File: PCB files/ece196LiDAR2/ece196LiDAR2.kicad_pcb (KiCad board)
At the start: 2 copper layers, 30.2 x 52.2 mm, 20 parts, among them J1 Conn_01x15_Socket, J10 Conn_01x03_Pin, J11 Conn_01x05_Pin, J12 Conn_01x01_Pin, J2 Conn_01x15_Socket, J3 LiDAR_IN, J4 Conn_01x01_Pin, J5 Conn_01x01_Pin, J6 Conn_01x01_Pin, J7 Conn_01x01_Pin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

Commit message: Updated PCB
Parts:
- moved J1 1.00 mm to (127.2, 112.4)
- moved SW1 1.00 mm to (127.0, 118.0)
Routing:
- net GND: track 91.3 -> 22.6 mm
- net +9V: track 59.7 -> 36.5 mm, vias 0 -> 2
- net Vov: track 15.9 -> 14.9 mm
- net VIN: track 6.91 -> 5.91 mm
- net TX0: track 9.81 -> 8.81 mm
- net +3v3: track 26.9 -> 25.9 mm
- net I2C/SCL: track 12.3 -> 11.3 mm
- added copper zone on B.Cu, net GND
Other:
- board size 30.2 x 52.2 mm -> 29.2 x 52.2 mm

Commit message: updated PCB again
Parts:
- moved C1 8.87 mm to (111.8, 93.1), turned to 90 degrees
- moved C3 8.83 mm to (111.8, 89.3), turned to -90 degrees
- moved C2 7.83 mm to (117.8, 93.1), turned to -90 degrees
- moved R1 7.37 mm to (117.8, 89.3), turned to 90 degrees
- moved L1 5.46 mm to (114.8, 93.6), turned to 180 degrees
- moved R2 4.33 mm to (114.8, 88.6), turned to 180 degrees
- moved U1 1.18 mm to (114.8, 91.1), turned to 0 degrees
- moved J10 0.75 mm to (107.5, 108.0)
- moved J3 0.75 mm to (121.5, 108.0)
- moved J8 0.75 mm to (116.8, 108.0)
- moved J9 0.75 mm to (112.2, 108.0)
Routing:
- net +5V: track 64.9 -> 8.96 mm, vias 0 -> 2
- net GND: track 22.6 -> 0.00 mm
- net Net-(U1-BST): track 16.7 -> 0.00 mm, vias 2 -> 0
- net Net-(U1-SW): track 13.5 -> 0.00 mm
- net Net-(U1-FB): track 4.51 -> 0.00 mm
- net +3v3: track 25.9 -> 29.2 mm, vias 0 -> 1
- net +9V: track 36.5 -> 39.8 mm, vias 2 -> 1
- net I2C/SDA: track 17.0 -> 16.0 mm
- added copper zone on F.Cu, net +5V
- added copper zone on F.Cu, net +9V
- added copper zone on F.Cu, net GND
- added copper zone on F.Cu, net Net-(U1-BST)
- added copper zone on F.Cu, net Net-(U1-FB)
- added copper zone on F.Cu, net Net-(U1-SW)

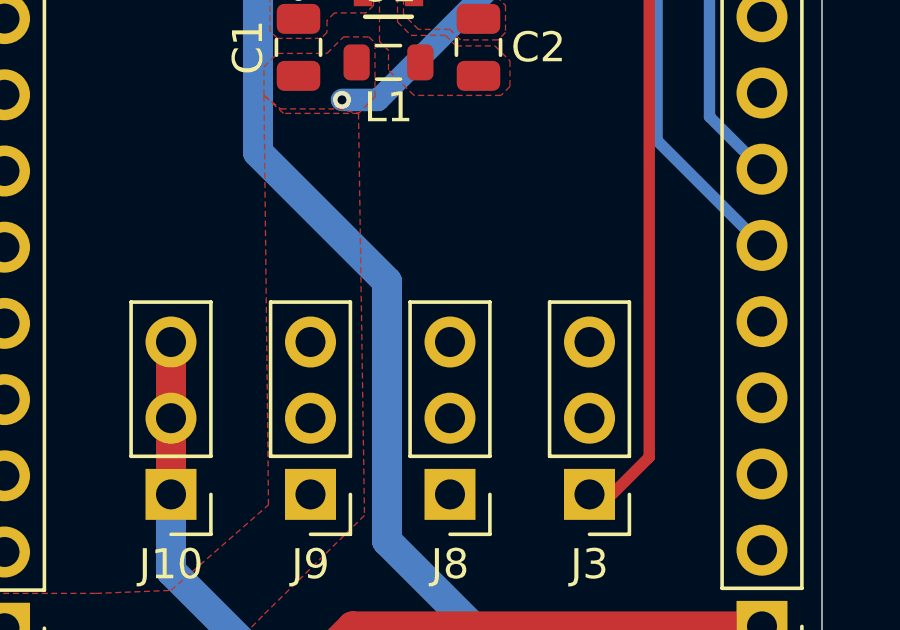
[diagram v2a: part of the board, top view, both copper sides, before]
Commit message: connected 5v trace
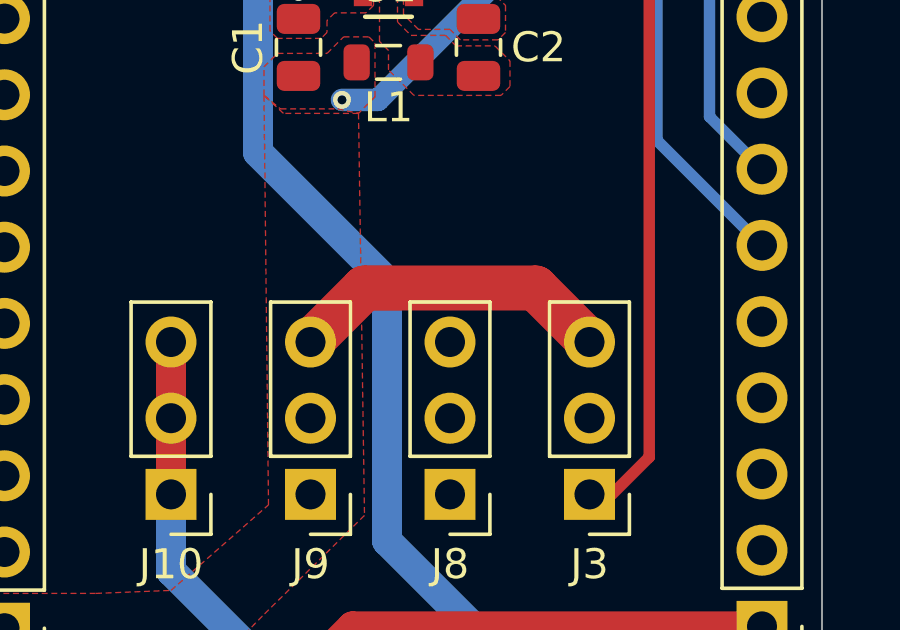
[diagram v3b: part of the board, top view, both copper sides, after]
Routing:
- net +5V: track 8.96 -> 19.8 mm
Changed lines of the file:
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@@
 		)
 		(property "Footprint" "vreg:SOT563_DIO"
-			(at 0 0 360)
+			(at 0 0 0)
 			(layer "F.Fab")
 			(hide yes)
@@
 		)
 		(property "Datasheet" "AP62150Z6-7"
-			(at 0 0 360)
+			(at 0 0 0)
 			(layer "F.Fab")
 			(hide yes)
@@
 		)
 		(property "Description" ""
-			(at 0 0 360)
+			(at 0 0 0)
 			(layer "F.Fab")
 			(hide yes)
@@
 		(tags "resistor")
 		(property "Reference" "R2"
-			(at 0 1.5 360)
+			(at 0 1.5 0)
 			(layer "F.SilkS")
 			(effects
@@
 		)
 		(property "Value" "10k"
-			(at 0 1.5 360)
+			(at 0 1.5 0)
 			(layer "F.Fab")
 			(effects
@@
 		)
 		(fp_text user "${REFERENCE}"
-			(at 0 0 360)
+			(at 0 0 0)
 			(layer "F.Fab")
 			(effects
@@
 		(tags "inductor")
 		(property "Reference" "L1"
-			(at 0 -1.5 360)
+			(at 0 -1.5 0)
 			(layer "F.SilkS")
 			(effects
@@
 		)
 		(property "Value" "3.3uH"
-			(at 0 1.55 360)
+			(at 0 1.55 0)
 			(layer "F.Fab")
 			(effects
@@
 		)
 		(fp_text user "${REFERENCE}"
-			(at 0 0 360)
+			(at 0 0 0)
 			(layer "F.Fab")
 			(effects
@@
 	)
 	(segment
+		(start 121.5 102.92)
+		(end 119.7 101.12)
+		(width 1.5)
+		(layer "F.Cu")
+		(net 1)
+	)
+	(segment
 		(start 117.8 90.2625)
 		(end 119.0375 90.2625)
@@
 		(layer "F.Cu")
 		(net 1)
+	)
+	(segment
+		(start 114 101.12)
+		(end 112.2 102.92)
+		(width 1.5)
+		(layer "F.Cu")
+		(net 1)
+	)
+	(segment
+		(start 119.7 101.12)
+		(end 114 101.12)
+		(width 1.5)
+		(layer "F.Cu")
+		(net 1)
